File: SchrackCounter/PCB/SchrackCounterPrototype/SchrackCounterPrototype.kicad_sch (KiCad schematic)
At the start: 0 parts

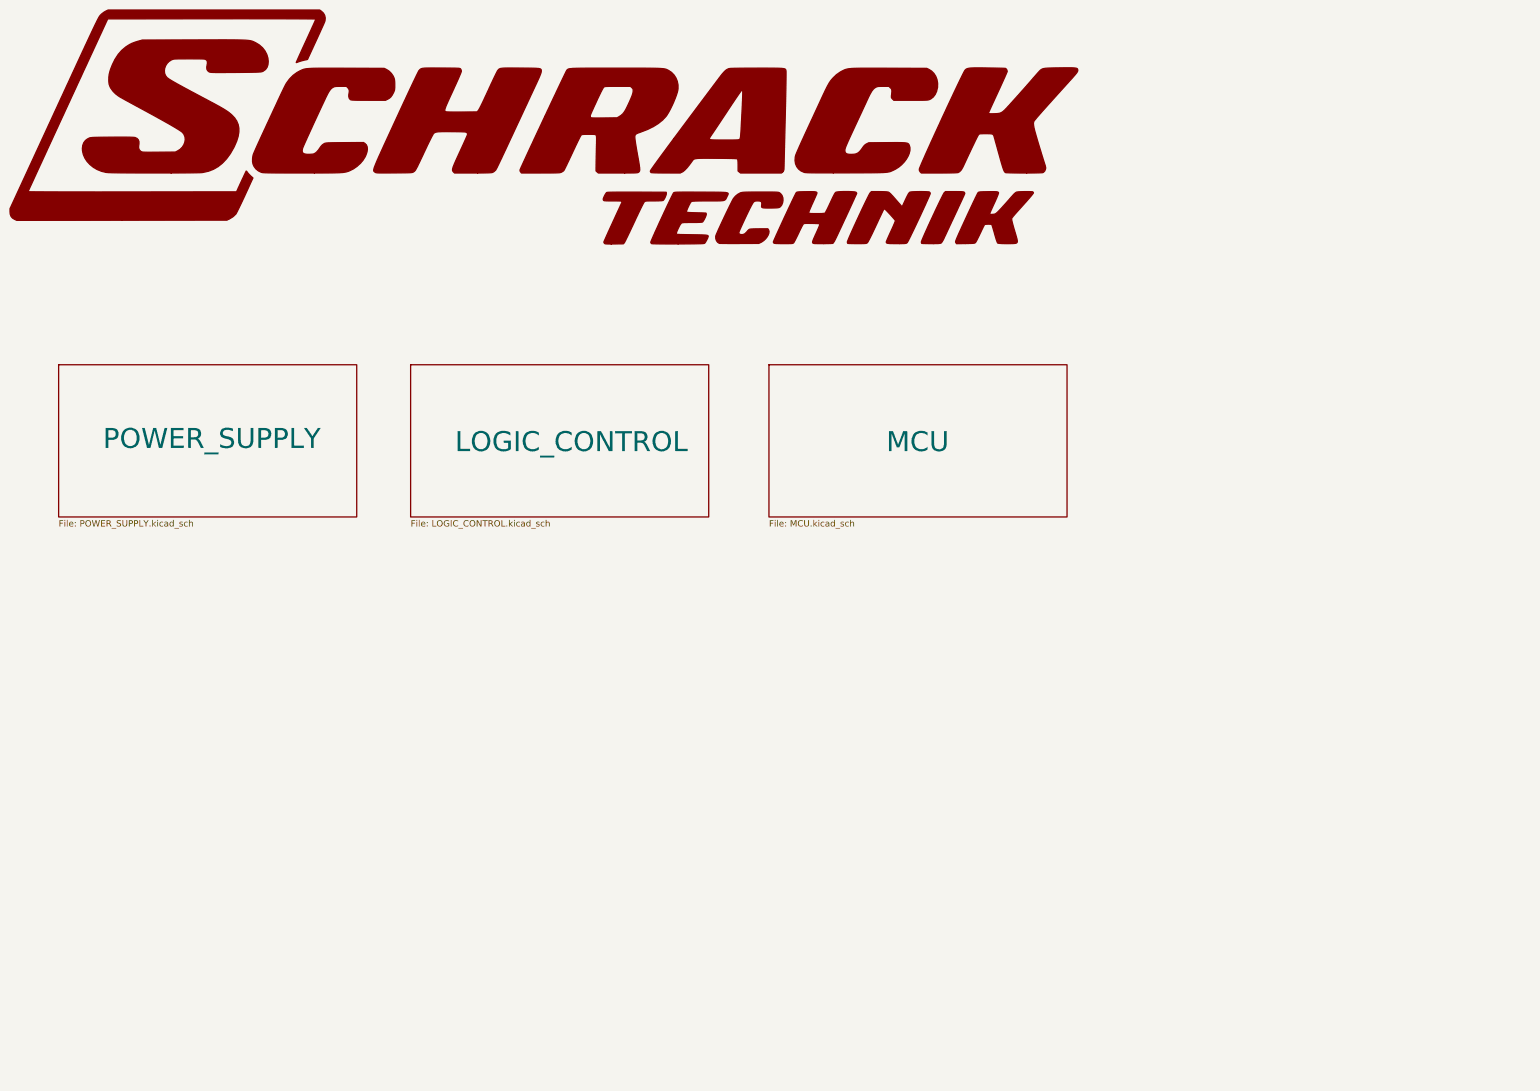
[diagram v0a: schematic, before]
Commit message: Schrackcounter Prototype update
Schematic + PCB update, final version
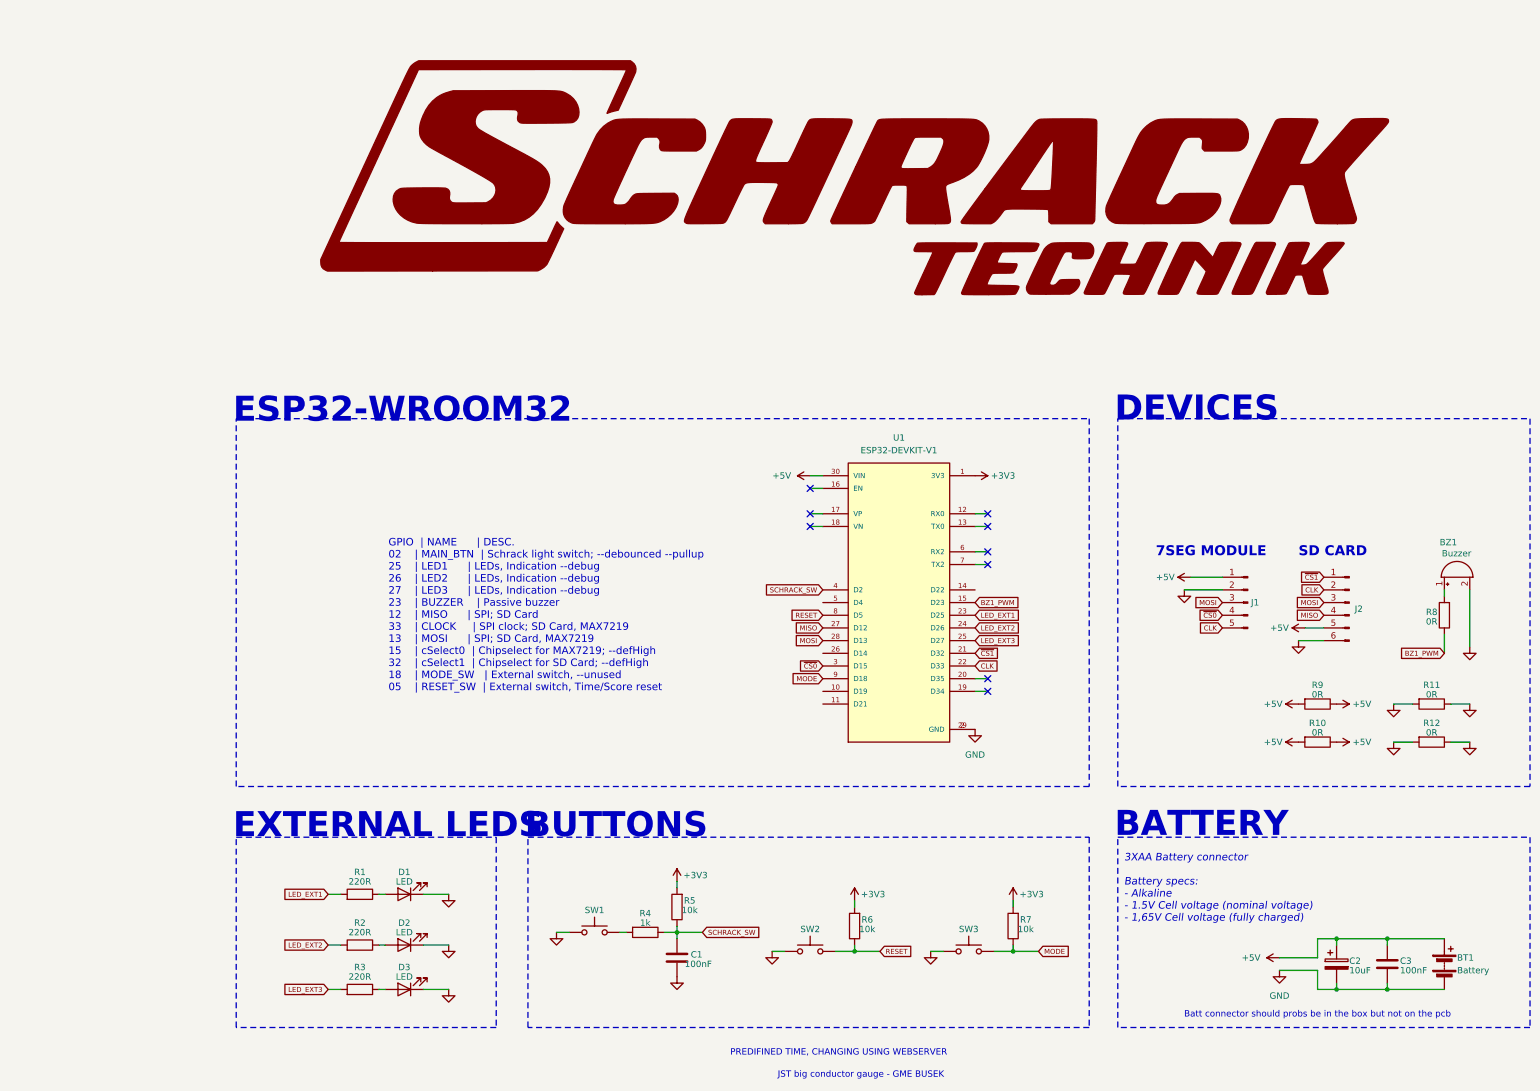
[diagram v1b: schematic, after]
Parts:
- added BT1: Battery, Schrack_brd:SOLDER_PADS, symbol Device:Battery
- added BZ1: Buzzer, Buzzer_Beeper:Buzzer_12x9.5RM7.6, symbol Device:Buzzer
- added C1, C3: 100nF, Capacitor_THT:C_Disc_D6.0mm_W2.5mm_P5.00mm, symbol Device:C
- added C2: 10uF, Capacitor_THT:CP_Radial_D6.3mm_P2.50mm, symbol Device:C_Polarized
- added D1, D2, D3: LED, LED_THT:LED_D5.0mm, symbol Device:LED
- added J1: Conn_01x05_Pin, Connector_PinHeader_2.54mm:PinHeader_1x05_P2.54mm_Vertical, symbol Connector:Conn_01x05_Pin
- added J2: Conn_01x06_Pin, Connector_PinHeader_2.54mm:PinHeader_1x06_P2.54mm_Vertical, symbol Connector:Conn_01x06_Pin
- added R1, R2, R3: 220R, Resistor_THT:R_Axial_DIN0207_L6.3mm_D2.5mm_P10.16mm_Horizontal, symbol Device:R
- added R10, R11, R12, R8, R9: 0R, Resistor_THT:R_Axial_DIN0207_L6.3mm_D2.5mm_P10.16mm_Horizontal, symbol Device:R
- added R4: 1k, Resistor_THT:R_Axial_DIN0207_L6.3mm_D2.5mm_P10.16mm_Horizontal, symbol Device:R
- added R5, R6, R7: 10k, Resistor_THT:R_Axial_DIN0207_L6.3mm_D2.5mm_P10.16mm_Horizontal, symbol Device:R
- added SW1: SW_Push, Schrack_brd:SOLDER_PADS, symbol Switch:SW_Push
- added SW2, SW3: SW_Push, Button_Switch_THT:SW_PUSH_6mm_H5mm, symbol Switch:SW_Push
- added U1: ESP32-DEVKIT-V1, Schrack_brd:MODULE_ESP32_DEVKIT_V1-NoPads-NoCopper, symbol SchrackThingy_library:ESP32-DEVKIT-V1
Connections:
- new net: BZ1.1 (+), R8.2
- new net: D1.2 (A), R1.1
- new net: D2.2 (A), R2.1
- new net: R4.2, SW1.2
- new net: D3.2 (A), R3.1
- new net +3V3: R5.2, R6.2, R7.2, U1.1 (3V3)
- new net +5V: BT1.1 (+), C2.1, C3.1, J1.1 (Pin_1), J2.5 (Pin_5), R10.1, R10.2, R9.1, R9.2, U1.30 (VIN)
- new net BZ1_PWM: R8.1, U1.15 (D23)
- new net CLK: J1.5 (Pin_5), J2.2 (Pin_2), U1.22 (D33)
- new net GND: BT1.2 (-), BZ1.2 (-), C1.1, C2.2, C3.2, D1.1 (K), D2.1 (K), D3.1 (K), J1.2 (Pin_2), J2.6 (Pin_6), R11.1, R11.2, R12.1, R12.2, SW1.1, SW2.1, SW3.1, U1.2 (GND), U1.29 (GND)
- new net LED_EXT1: R1.2, U1.23 (D25)
- new net LED_EXT2: R2.2, U1.24 (D26)
- new net LED_EXT3: R3.2, U1.25 (D27)
- new net MISO: J2.4 (Pin_4), U1.27 (D12)
- new net MODE: R7.1, SW3.2, U1.9 (D18)
- new net MOSI: J1.3 (Pin_3), J2.3 (Pin_3), U1.28 (D13)
- new net RESET: R6.1, SW2.2, U1.8 (D5)
- new net SCHRACK_SW: C1.2, R4.1, R5.1, U1.4 (D2)
- new net ~{CS0}: J1.4 (Pin_4), U1.3 (D15)
- new net ~{CS1}: J2.1 (Pin_1), U1.21 (D32)
- no-connect marks 0 -> 9
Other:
- removed sheet LOGIC_CONTROL
- removed sheet MCU
- removed sheet POWER_SUPPLY
- note added: "3XAA Battery connector Battery specs: - Alkaline - 1.5V Cell voltage (nominal voltage) - 1,65V Cell voltage (fully charged)"
- note added: "7SEG MODULE"
- note added: "BATTERY"
- note added: "BUTTONS"
- note added: "Batt connector should probs be in the box but not on the pcb"
- note added: "DEVICES"
- note added: "ESP32-WROOM32"
- note added: "EXTERNAL LEDS"
- note added: "GPIO | NAME | DESC. 02 | MAIN_BTN | Schrack light switch; --debounced --pullup 25 | LED1 | LEDs, Indication --debug 26 | LED2 | LEDs, Indication --debug 27 | LED3 | LEDs, Indication --debug 23 | BUZZER | Passive buzzer 12 | MISO | SPI; SD Card 33 | CLOCK | SPI clock; SD Card, MAX7219 13 | MOSI | SPI; SD Card, MAX7219 15 | cSelect0 | Chipselect for MAX7219; --defHigh 32 | cSelect1 | Chipselect for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"
- note added: "JST big conductor gauge - GME BUSEK"
- note added: "PREDIFINED TIME, CHANGING USING WEBSERVER"
- note added: "SD CARD"

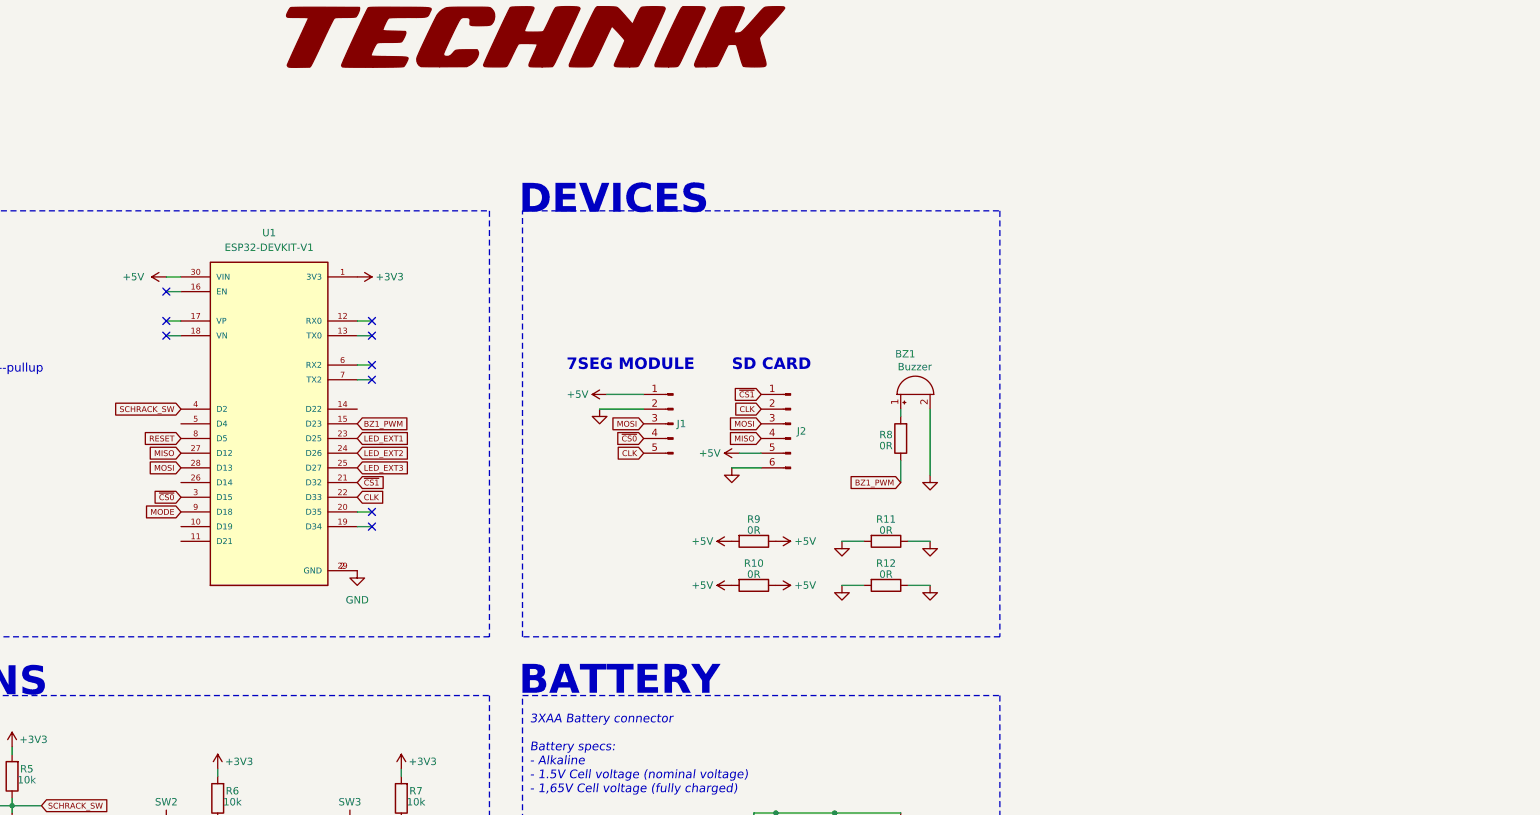
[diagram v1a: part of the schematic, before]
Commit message: Schrack prototype updated for s3
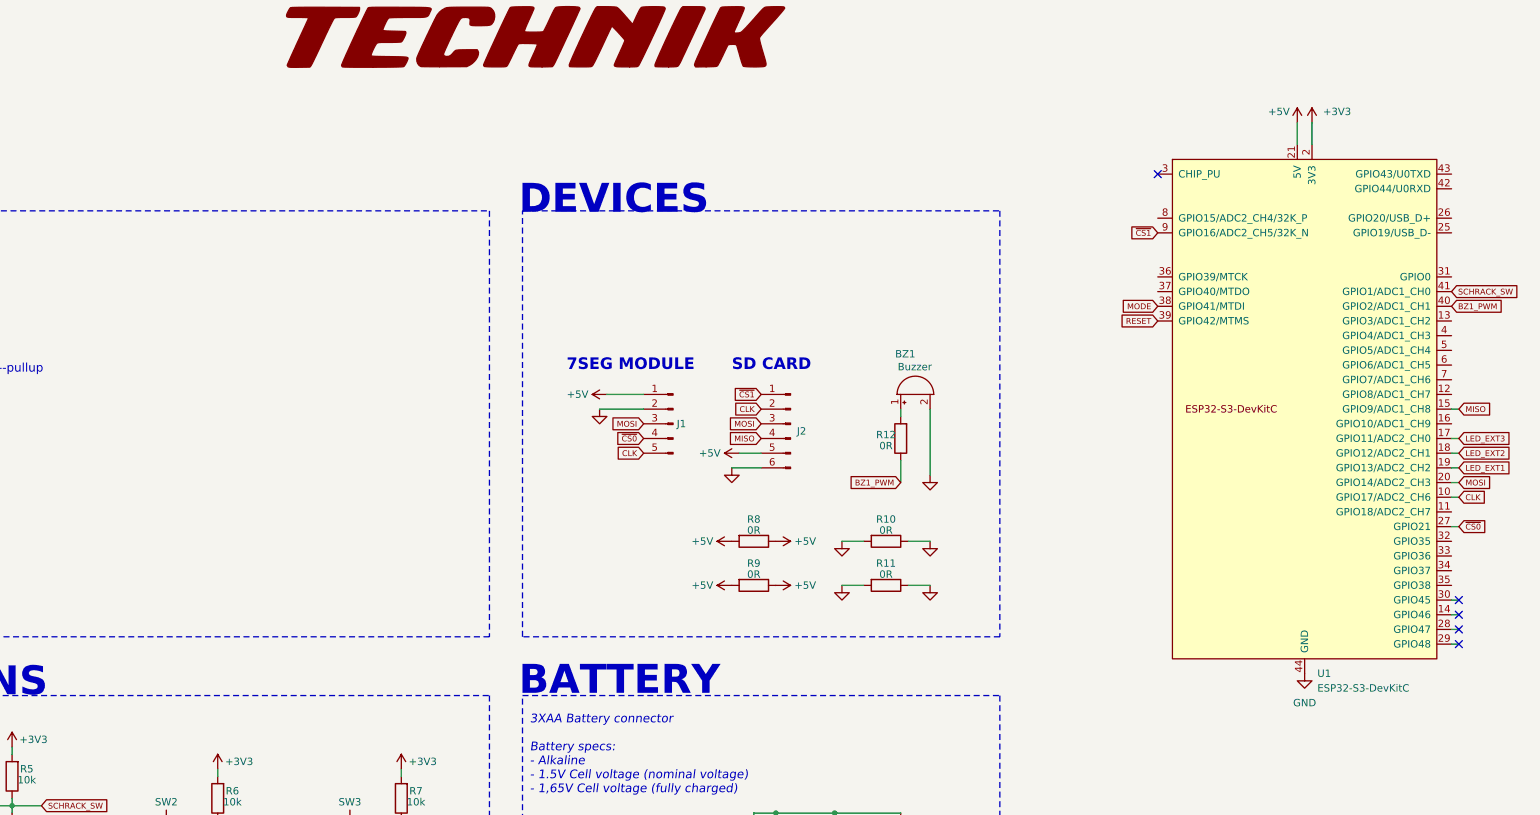
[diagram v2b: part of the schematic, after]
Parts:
- removed U1: ESP32-DEVKIT-V1, Schrack_brd:MODULE_ESP32_DEVKIT_V1-NoPads-NoCopper, symbol SchrackThingy_library:ESP32-DEVKIT-V1
- added U1: ESP32-S3-DevKitC, PCM_Espressif:ESP32-S3-DevKitC, symbol PCM_Espressif:ESP32-S3-DevKitC
- renumbered R11 to R10, R12 to R11, R8 to R12, R9 to R8, R10 to R9
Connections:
- net +3V3: now also U1.1 (3V3), U1.2 (3V3)
- net +5V: now also U1.21 (5V)
- net BZ1_PWM: now also U1.40 (GPIO2/ADC1_CH1)
- net CLK: now also U1.10 (GPIO17/ADC2_CH6)
- net GND: now also U1.22 (GND), U1.23 (GND), U1.24 (GND), U1.44 (GND)
- net LED_EXT1: now also U1.19 (GPIO13/ADC2_CH2)
- net LED_EXT2: now also U1.18 (GPIO12/ADC2_CH1)
- net LED_EXT3: now also U1.17 (GPIO11/ADC2_CH0)
- net MISO: now also U1.15 (GPIO9/ADC1_CH8)
- net MODE: now also U1.38 (GPIO41/MTDI)
- net MOSI: now also U1.20 (GPIO14/ADC2_CH3)
- net RESET: now also U1.39 (GPIO42/MTMS)
- net SCHRACK_SW: now also U1.41 (GPIO1/ADC1_CH0)
- net ~{CS0}: now also U1.27 (GPIO21)
- net ~{CS1}: now also U1.9 (GPIO16/ADC2_CH5/32K_N)
- no-connect marks 9 -> 5
